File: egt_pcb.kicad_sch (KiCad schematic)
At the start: 7 parts, among them J6 EGT_sensor, U3 MAX31856

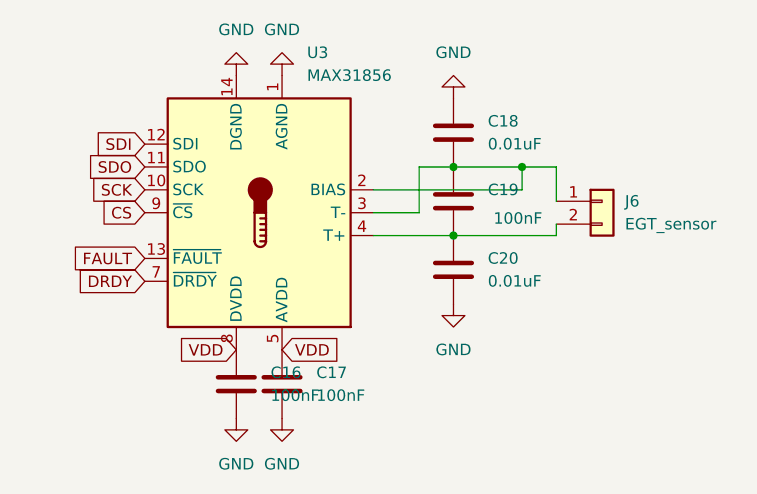
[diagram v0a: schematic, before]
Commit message: Optimized PCB layout. Added images
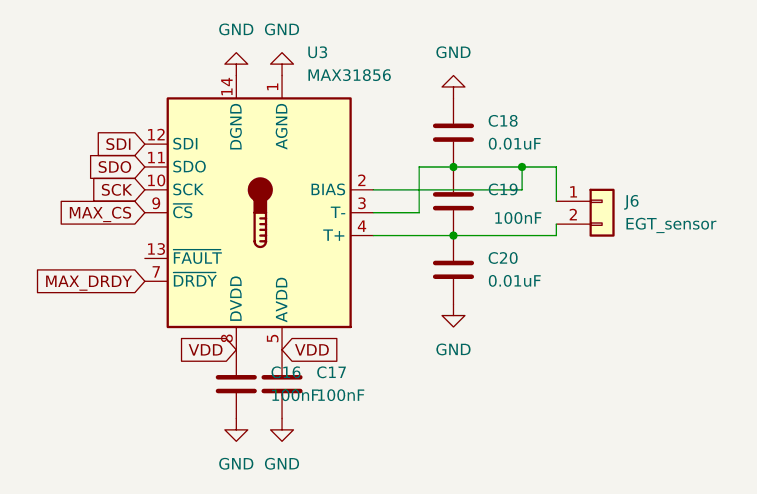
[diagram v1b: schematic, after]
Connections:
- net CS renamed MAX_CS
- net DRDY renamed MAX_DRDY
- net FAULT: no longer names the net of U3.13 (~{FAULT})
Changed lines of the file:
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@@
 		)
 	)
-	(global_label "CS"
+	(global_label "MAX_CS"
 		(shape input)
 		(at 115.57 99.06 180)
@@
 		)
 		(property "Intersheetrefs" "${INTERSHEET_REFS}"
-			(at 110.1053 99.06 0)
-			(effects
-				(font
-					(size 1.27 1.27)
-				)
-				(justify right)
-				(hide yes)
-			)
-		)
-	)
-	(global_label "FAULT"
-		(shape input)
-		(at 115.57 104.14 180)
-		(fields_autoplaced yes)
-		(effects
-			(font
-				(size 1.27 1.27)
-			)
-			(justify right)
-		)
-		(property "Intersheetrefs" "${INTERSHEET_REFS}"
-			(at 107.0814 104.14 0)
+			(at 105.3882 99.06 0)
 			(effects
 				(font
@@
 		)
 	)
-	(global_label "DRDY"
+	(global_label "MAX_DRDY"
 		(shape input)
 		(at 115.57 106.68 180)
@@
 		)
 		(property "Intersheetrefs" "${INTERSHEET_REFS}"
-			(at 107.6862 106.68 0)
+			(at 102.9691 106.68 0)
 			(effects
 				(font

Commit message: THT caps to MLCC as per TS1117B datasheet. STM32 ref caps as well
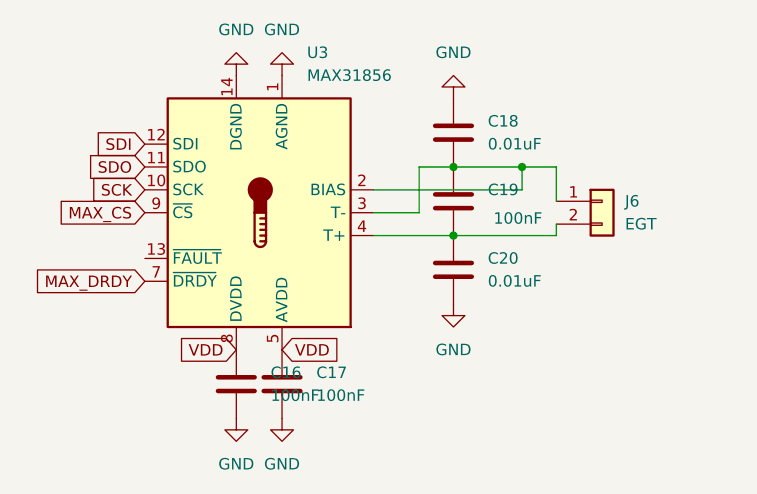
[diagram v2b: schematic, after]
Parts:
- J6: value EGT_sensor -> EGT
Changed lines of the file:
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@@
 			)
 		)
-		(property "Value" "EGT_sensor"
+		(property "Value" "EGT"
 			(at 168.91 100.3299 0)
 			(effects

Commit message: Changed footprints to larger ones and for general unity of footprints
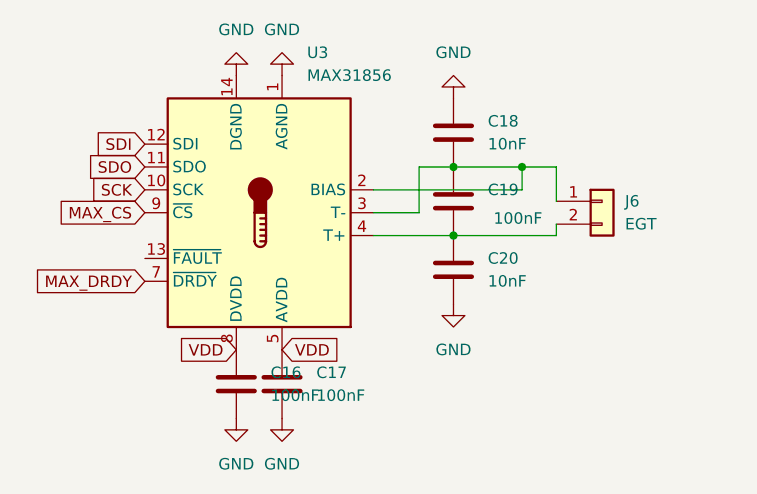
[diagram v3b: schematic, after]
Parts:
- C18, C20: value 0.01uF -> 10nF; footprint Capacitor_SMD:C_0402_1005Metric_Pad0.74x0.62mm_HandSolder -> Capacitor_SMD:C_0805_2012Metric_Pad1.18x1.45mm_HandSolder
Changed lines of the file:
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@@
 			)
 		)
-		(property "Value" "0.01uF"
+		(property "Value" "10nF"
 			(at 153.67 91.4399 0)
 			(effects
@@
 			)
 		)
-		(property "Footprint" "Capacitor_SMD:C_0402_1005Metric_Pad0.74x0.62mm_HandSolder"
+		(property "Footprint" "Capacitor_SMD:C_0805_2012Metric_Pad1.18x1.45mm_HandSolder"
 			(at 150.8252 93.98 0)
 			(effects
@@
 			)
 		)
-		(property "Value" "0.01uF"
+		(property "Value" "10nF"
 			(at 153.67 106.6799 0)
 			(effects
@@
 			)
 		)
-		(property "Footprint" "Capacitor_SMD:C_0402_1005Metric_Pad0.74x0.62mm_HandSolder"
+		(property "Footprint" "Capacitor_SMD:C_0805_2012Metric_Pad1.18x1.45mm_HandSolder"
 			(at 150.8252 109.22 0)
 			(effects
